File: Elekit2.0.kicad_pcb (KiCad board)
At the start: 2 copper layers, 100 x 58.5 mm, 55 parts, among them Q1 S8050, Q2 AO3401A, Q3 S8050, Q4 2N7002, SW1 SW_Push, U1 MY-2032-12, U2 TYPE-C_16PIN_2MD(073), U3 MY-2032-12, U4 74HC595, U5 XC6206P332MR, U6 TS-1187A-B-A-B, U7 TS-1187A-B-A-B, U8 ESP32-C3-WROOM-02-N4(4MB), U9 SRV05-4-P-T7

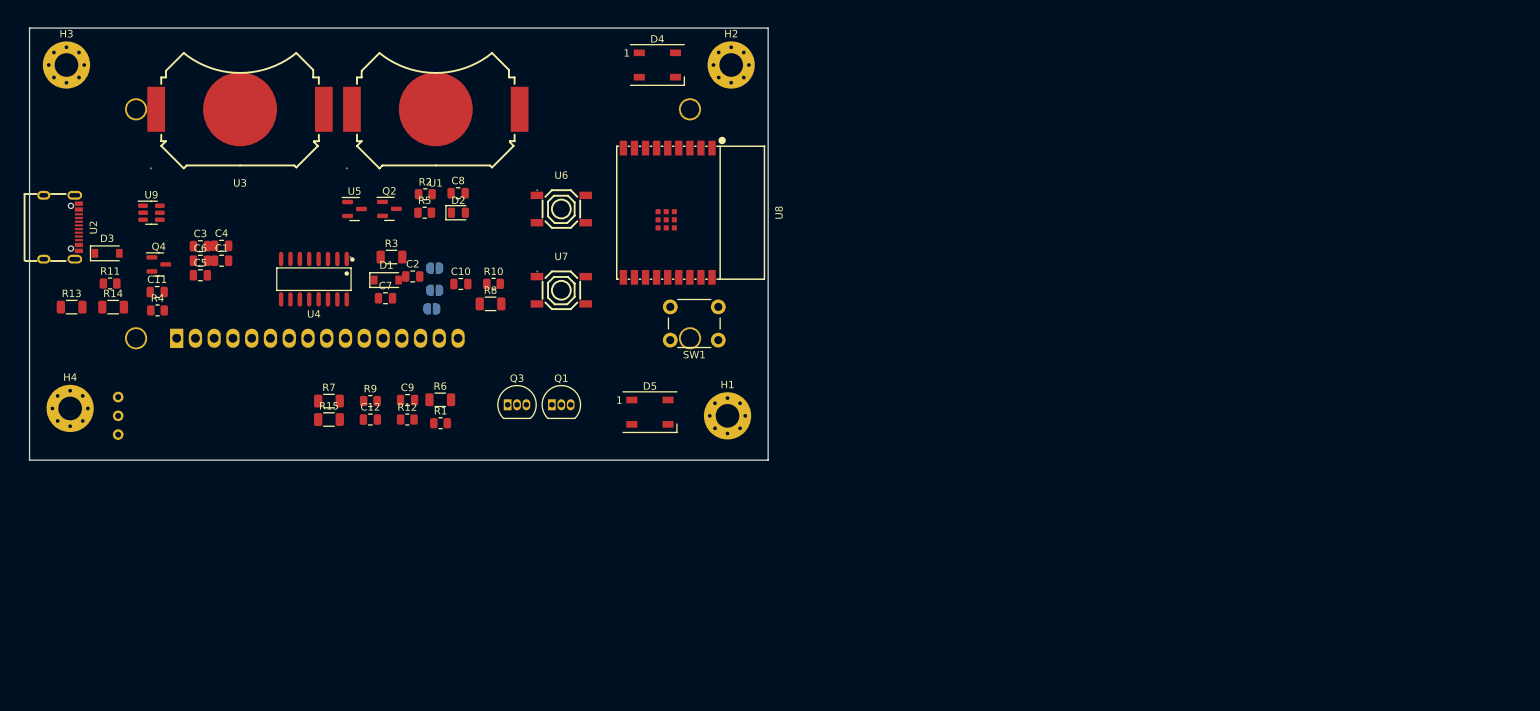
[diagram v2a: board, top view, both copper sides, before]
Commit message: Add H bridge motor controllers and create first draft of pcb
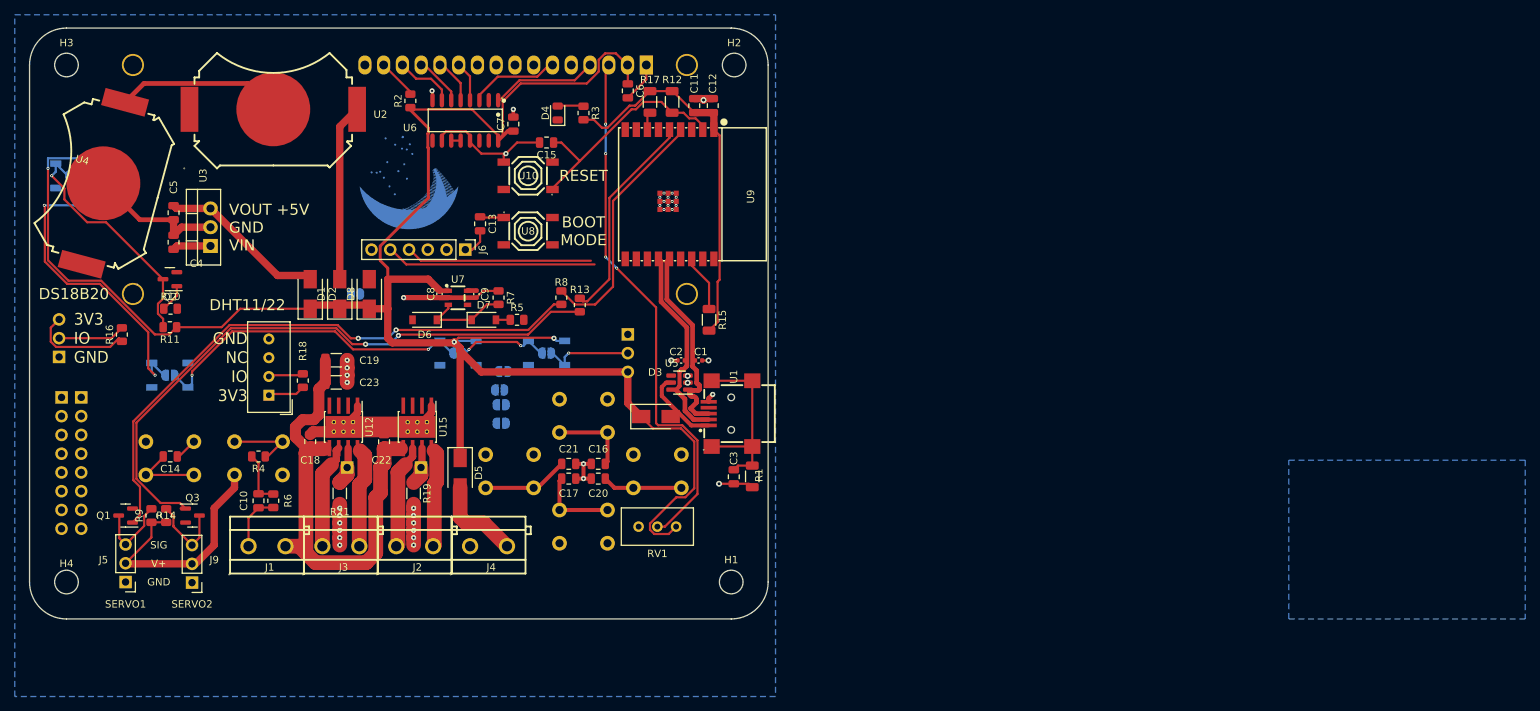
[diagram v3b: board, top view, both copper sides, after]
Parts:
- removed Q4: 2N7002, Package_TO_SOT_SMD:SOT-23
- added C13: 0.1u, Capacitor_SMD:C_0805_2012Metric, F.Cu at (81.0, 46.5)
- added C14: 0.1u, Capacitor_SMD:C_0805_2012Metric, F.Cu at (39.0, 78.0)
- added C15: 0.1u, Capacitor_SMD:C_0805_2012Metric, F.Cu at (90.0, 35.5)
- added C16: 0.1u, Capacitor_SMD:C_0805_2012Metric, F.Cu at (97.0, 79.0)
- added C17: 0.1u, Capacitor_SMD:C_0805_2012Metric, F.Cu at (93.0, 81.0)
- added C18: 0.1u, Capacitor_SMD:C_0805_2012Metric, F.Cu at (58.0, 76.0)
- added C19: 10u 50V, Capacitor_SMD:C_1206_3216Metric, F.Cu at (61.5, 65.0)
- added C20: 0.1u, Capacitor_SMD:C_0805_2012Metric, F.Cu at (97.0, 81.0)
- added C21: 0.1u, Capacitor_SMD:C_0805_2012Metric, F.Cu at (93.0, 79.0)
- added C22: 0.1u, Capacitor_SMD:C_0805_2012Metric, F.Cu at (68.0, 76.0)
- added C23: 10u 50V, Capacitor_SMD:C_1206_3216Metric, F.Cu at (61.5, 68.0)
- added D10: WS2812B, LED_SMD:LED_WS2812B_PLCC4_5.0x5.0mm_P3.2mm, B.Cu at (39.0, 67.0)
- added D11: WS2812B, LED_SMD:LED_WS2812B_PLCC4_5.0x5.0mm_P3.2mm, B.Cu at (78.0, 64.0)
- added D12: WS2812B, LED_SMD:LED_WS2812B_PLCC4_5.0x5.0mm_P3.2mm, B.Cu at (90.0, 64.0)
- added D6: 1N4148W, Diode_SMD:D_SOD-123, F.Cu at (73.5, 59.5)
- added D7: 1N4148W, Diode_SMD:D_SOD-123, F.Cu at (81.5, 59.5)
- added D8: SS34, Diode_SMD:D_SMA, F.Cu at (66.0, 56.0)
- added D9: WS2812B, LED_SMD:LED_WS2812B_PLCC4_5.0x5.0mm_P3.2mm, B.Cu at (26.0, 40.0)
- added J1: Screw_Terminal_01x02, 0_JLCPCB_Footprints:CONN-TH_P5.00_KF301-5.0-2P, F.Cu at (52.5, 90.0)
- added J10: Conn_01x03_Male, Connector_PinHeader_2.54mm:PinHeader_1x03_P2.54mm_Vertical, B.Cu at (101.0, 61.5)
- added J11: DS18B20 temperature sensor, Connector_PinHeader_2.54mm:PinHeader_1x03_P2.54mm_Vertical, B.Cu at (24.0, 64.5)
- added J12: Conn_01x01_Male, Connector_PinHeader_2.54mm:PinHeader_1x01_P2.54mm_Vertical, F.Cu at (63.0, 79.5)
- added J13: Conn_01x01_Male, 0_JLCPCB_Footprints:PinHeader_1x01_P2.54mm_Vertical, F.Cu at (73.0, 79.5)
- added J2: Screw_Terminal_01x02, 0_JLCPCB_Footprints:CONN-TH_P5.00_KF301-5.0-2P, F.Cu at (72.5, 90.0)
- added J3: Screw_Terminal_01x02, 0_JLCPCB_Footprints:CONN-TH_P5.00_KF301-5.0-2P, F.Cu at (62.5, 90.0)
- added J4: Screw_Terminal_01x02, 0_JLCPCB_Footprints:CONN-TH_P5.00_KF301-5.0-2P, F.Cu at (82.5, 90.0)
- added J5: Conn_01x03_Male, Connector_PinHeader_2.54mm:PinHeader_1x03_P2.54mm_Vertical, F.Cu at (33.0, 95.0)
- added J6: Conn_01x06_Male, Connector_PinHeader_2.54mm:PinHeader_1x06_P2.54mm_Vertical, F.Cu at (79.0, 50.0)
- added J7: Conn_01x08, Connector_PinHeader_2.54mm:PinHeader_1x08_P2.54mm_Vertical, B.Cu at (27.0, 70.0)
- added J8: Conn_01x08, Connector_PinHeader_2.54mm:PinHeader_1x08_P2.54mm_Vertical, B.Cu at (24.3, 70.0)
- added J9: Conn_01x03_Male, Connector_PinHeader_2.54mm:PinHeader_1x03_P2.54mm_Vertical, F.Cu at (42.0, 95.1)
- added JP4: Power LED, Jumper:SolderJumper-2_P1.3mm_Open_RoundedPad1.0x1.5mm, B.Cu at (83.7, 69.0)
- added JP5: led bypass, Jumper:SolderJumper-2_P1.3mm_Open_RoundedPad1.0x1.5mm, B.Cu at (64.2, 56.0)
- added JP6: led bypass, Jumper:SolderJumper-2_P1.3mm_Open_RoundedPad1.0x1.5mm, B.Cu at (26.0, 40.0)
- added JP7: led bypass, Jumper:SolderJumper-2_P1.3mm_Open_RoundedPad1.0x1.5mm, B.Cu at (39.0, 67.0)
- added JP8: led bypass, Jumper:SolderJumper-2_P1.3mm_Open_RoundedPad1.0x1.5mm, B.Cu at (78.0, 64.0)
- added JP9: led bypass, Jumper:SolderJumper-2_P1.3mm_Open_RoundedPad1.0x1.5mm, B.Cu at (90.0, 64.0)
- added LOGO1: CASTOR, 0_JLCPCB_Footprints:Castor logo, B.Cu at (78.5, 33.4)
- added R16: 4.7k, Resistor_SMD:R_0805_2012Metric, F.Cu at (32.5, 61.5)
- added R17: 10k, Resistor_SMD:R_1206_3216Metric, F.Cu at (104.0, 30.0)
- added R18: 10k, Resistor_SMD:R_0805_2012Metric, F.Cu at (57.0, 67.7)
- added R19: 0R, Resistor_SMD:R_1206_3216Metric, F.Cu at (72.0, 83.0)
- added R21: 0R, Resistor_SMD:R_1206_3216Metric, F.Cu at (62.0, 83.0)
- added SW2: SW_Push, Button_Switch_THT:SW_PUSH_6mm, B.Cu at (42.2, 76.0)
- added SW3: SW_Push, Button_Switch_THT:SW_PUSH_6mm, B.Cu at (98.2, 70.2)
- added SW4: SW_Push, Button_Switch_THT:SW_PUSH_6mm, B.Cu at (91.8, 89.8)
- added SW5: SW_Push, Button_Switch_THT:SW_PUSH_6mm, B.Cu at (108.2, 77.8)
- added SW6: SW_Push, Button_Switch_THT:SW_PUSH_6mm, B.Cu at (88.2, 77.8)
- added U10: TS-1187A-B-A-B, 0_JLCPCB_Footprints:SW-SMD_4P-L5.1-W5.1-P3.70-LS6.5-TL-2, F.Cu at (87.5, 40.0)
- added U11: DHT11, Sensor:Aosong_DHT11_5.5x12.0_P2.54mm, F.Cu at (52.4, 69.7)
- added U12: DRV8870DDA, Package_SO:Texas_HTSOP-8-1EP_3.9x4.9mm_P1.27mm_EP2.95x4.9mm_Mask2.4x3.1mm_ThermalVias, F.Cu at (62.5, 74.0)
- added U15: DRV8870DDA, Package_SO:Texas_HTSOP-8-1EP_3.9x4.9mm_P1.27mm_EP2.95x4.9mm_Mask2.4x3.1mm_ThermalVias, F.Cu at (72.5, 74.0)
- C1, C2: value 0.1u -> 0.1u 50V; footprint Capacitor_SMD:C_0805_2012Metric -> Capacitor_SMD:C_0402_1005Metric
- C10: value 0.1u -> 1u
- C3: value 0.1u -> 4.7n
- C4: value 4.7n -> 0.47u 50v
- C6, C7: value 1u -> 0.1u
- C8: value 1u -> 1u 25V; footprint Capacitor_SMD:C_0805_2012Metric -> Capacitor_SMD:C_0402_1005Metric
- C9: value 0.1u -> 1u 25V; footprint Capacitor_SMD:C_0805_2012Metric -> Capacitor_SMD:C_0402_1005Metric
- D1, D3: value B5819W -> SS34; footprint Diode_SMD:D_SOD-123 -> Diode_SMD:D_SMA
- D2: value LED -> SS34; footprint LED_SMD:LED_0805_2012Metric -> Diode_SMD:D_SMA
- D4: value WS2812B -> LED; footprint LED_SMD:LED_WS2812B_PLCC4_5.0x5.0mm_P3.2mm -> LED_SMD:LED_0805_2012Metric
- D5: value WS2812B -> SS34; footprint LED_SMD:LED_WS2812B_PLCC4_5.0x5.0mm_P3.2mm -> Diode_SMD:D_SMA
- H1, H2, H3, H4: footprint MountingHole:MountingHole_3.2mm_M3_Pad_Via -> MountingHole:MountingHole_3.2mm_M3
- JP1: value Power LED -> Latch bypass
- JP2: value Latch bypass -> VIN DIODE BYPASS
- JP3: value Power latch -> Latch control
- Q1, Q3: value S8050 -> 2N7002; footprint Package_TO_SOT_THT:TO-92_Inline -> Package_TO_SOT_SMD:SOT-23
- Q2: value AO3401A -> 2N7002
- R1: value 1k -> 1M; footprint Resistor_SMD:R_0805_2012Metric -> Resistor_SMD:R_1206_3216Metric
- R11: value 1k -> 5.1k
- R12: value 5.1k -> 10k; footprint Resistor_SMD:R_0805_2012Metric -> Resistor_SMD:R_1206_3216Metric
- R13, R14, R8: value 10k -> 1k; footprint Resistor_SMD:R_1206_3216Metric -> Resistor_SMD:R_0805_2012Metric
- R2: value 5.1k -> 220R
- R3: value 1M -> 1k; footprint Resistor_SMD:R_1206_3216Metric -> Resistor_SMD:R_0805_2012Metric
- R4: value 220R -> 10k
- R5: value 5.1k -> 1k
- R6: footprint Resistor_SMD:R_1206_3216Metric -> Resistor_SMD:R_0805_2012Metric
- R7: value 10k -> 1M; footprint Resistor_SMD:R_1206_3216Metric -> Resistor_SMD:R_0805_2012Metric
- RV1: moved to F.Cu
- SW1: moved to B.Cu
- U1: value MY-2032-12 -> MINI_5PTP; footprint 0_JLCPCB_Footprints:BAT-SMD_MY-2032-12 -> 0_JLCPCB_Footprints:MINI-USB-SMD_MINI-5PTP
- U2: value TYPE-C_16PIN_2MD(073) -> MY-2032-12; footprint 0_JLCPCB_Footprints:USB-C-SMD_TYPE-C-6PIN-2MD-073 -> 0_JLCPCB_Footprints:BAT-SMD_MY-2032-12
- U3: value MY-2032-12 -> L7805; footprint 0_JLCPCB_Footprints:BAT-SMD_MY-2032-12 -> Package_TO_SOT_THT:TO-220-3_Vertical
- U4: value 74HC595 -> MY-2032-12; footprint 0_JLCPCB_Footprints:SOIC-16_L9.9-W3.9-P1.27-LS6.0-BL -> 0_JLCPCB_Footprints:BAT-SMD_MY-2032-12
- U5: value XC6206P332MR -> SRV05-4-P-T7; footprint Package_TO_SOT_SMD:SOT-23 -> Package_TO_SOT_SMD:SOT-23-6
- U6: value TS-1187A-B-A-B -> 74HC595; footprint 0_JLCPCB_Footprints:SW-SMD_4P-L5.1-W5.1-P3.70-LS6.5-TL-2 -> 0_JLCPCB_Footprints:SOIC-16_L9.9-W3.9-P1.27-LS6.0-BL
- U7: value TS-1187A-B-A-B -> ME6211C33M5G-N; footprint 0_JLCPCB_Footprints:SW-SMD_4P-L5.1-W5.1-P3.70-LS6.5-TL-2 -> 0_JLCPCB_Footprints:SOT-23-5_L3.0-W1.7-P0.95-LS2.8-BR
- U8: value ESP32-C3-WROOM-02-N4(4MB) -> TS-1187A-B-A-B; footprint 0_JLCPCB_Footprints:BULETM-SMD_ESPRESSIF_ESP32-C3-WROOM-02-N4-4MB -> 0_JLCPCB_Footprints:SW-SMD_4P-L5.1-W5.1-P3.70-LS6.5-TL-2
- U9: value SRV05-4-P-T7 -> ESP32-C3-WROOM-02-N4(4MB); footprint Package_TO_SOT_SMD:SOT-23-6 -> 0_JLCPCB_Footprints:BULETM-SMD_ESPRESSIF_ESP32-C3-WROOM-02-N4-4MB
- moved C3 78.7 mm to (115.4, 80.8), turned to -90 degrees
- moved D3 77.5 mm to (104.8, 72.6)
- moved C11 77.0 mm to (110.0, 30.5), turned to 90 degrees
- moved DS1 73.6 mm to (103.5, 25.0), turned to 180 degrees
- moved RV1 71.6 mm to (102.5, 87.5), turned to 180 degrees
- moved U9 70.2 mm to (106.6, 42.5), turned to -90 degrees
- moved R13 68.8 mm to (94.5, 57.5), turned to 90 degrees
- moved C1 66.0 mm to (110.6, 65.0)
- moved C12 62.9 mm to (112.5, 30.5), turned to -90 degrees
- moved C6 62.3 mm to (101.0, 28.5), turned to -90 degrees
- moved SW1 60.6 mm to (54.2, 76.0)
- moved Q1 59.6 mm to (33.0, 86.0), turned to 180 degrees
- moved U1 57.2 mm to (114.9, 72.2), turned to 90 degrees
- moved R12 56.0 mm to (107.0, 30.0), turned to 90 degrees
- moved R15 53.2 mm to (112.0, 59.5), turned to -90 degrees
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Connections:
- C1 pad 1: /VBUS -> /D+
- C10 pad 1: /CHIP_PU -> /BTN
- C12 pad 1: +3.3V -> GND
- C12 pad 2: GND -> +3.3V
- C2 pad 2: /D+ -> /D-
- C3 pad 1: GND -> Net-(C3-Pad1)
- C3 pad 2: /D- -> GND
- C4 pad 1: Net-(C4-Pad1) -> GND
- C4 pad 2: GND -> /HVBUS
- C5 pad 1: /VBUS -> GND
- C5 pad 2: GND -> Net-(C5-Pad2)
- C6 pad 1: Net-(C6-Pad1) -> /VBUS
- C7 pad 1: Net-(C7-Pad1) -> /VBUS
- C8 pad 1: +3.3V -> GND
- C8 pad 2: GND -> /VBUS
- C9 pad 1: /GPIO9 -> +3.3V
- D2 pad 1: GND -> /VBUS
- D2 pad 2: Net-(D2-Pad2) -> Net-(C5-Pad2)
- D4 pad 1: /VBUS -> Net-(D4-Pad1)
- D5 pad 2: unconnected-(D5-Pad2) -> Net-(D5-Pad2)
- JP1 pad 1: Net-(D2-Pad2) -> /EN_LDO
- JP1 pad 2: Net-(JP1-Pad2) -> /VBUS
- JP2 pad 1: Net-(C6-Pad1) -> /VBUS
- JP2 pad 2: /VBUS -> Net-(D5-Pad2)
- JP3 pad 1: /GPIO4 -> Net-(JP3-Pad1)
- JP3 pad 2: Net-(JP3-Pad2) -> /GPIO4
- Q1 pad 1: /RTS -> Net-(Q1-Pad1)
- Q1 pad 2: Net-(Q1-Pad2) -> GND
- Q1 pad 3: /CHIP_PU -> /SERVO1
- Q2 pad 1: Net-(C7-Pad1) -> Net-(Q2-Pad1)
- Q2 pad 2: /VBUS -> GND
- Q2 pad 3: Net-(C6-Pad1) -> Net-(D9-Pad4)
- Q3 pad 1: /DTR -> Net-(Q3-Pad1)
- Q3 pad 2: Net-(Q3-Pad2) -> GND
- Q3 pad 3: /GPIO9 -> /SERVO2
- R1 pad 1: Net-(JP1-Pad2) -> Net-(C3-Pad1)
- R1 pad 2: +3.3V -> GND
- R10 pad 1: Net-(C7-Pad1) -> Net-(Q2-Pad1)
- R10 pad 2: Net-(JP3-Pad2) -> /GPIO5
- R11 pad 1: Net-(Q4-Pad1) -> /VBUS
- R11 pad 2: /GPIO5 -> Net-(D9-Pad4)
- R12 pad 1: /VBUS -> /CHIP_PU
- R12 pad 2: Net-(D4-Pad4) -> +3.3V
- R13 pad 1: /CHIP_PU -> Net-(Q3-Pad1)
- R13 pad 2: +3.3V -> /GPIO6
- R14 pad 1: /GPIO2 -> /VBUS
- R14 pad 2: +3.3V -> /SERVO2
- R15 pad 1: /GPIO8 -> /GPIO2
- R2 pad 1: GND -> /VBUS
- R2 pad 2: Net-(R2-Pad2) -> Net-(DS1-Pad15)
- R3 pad 1: Net-(C4-Pad1) -> Net-(D4-Pad2)
- R3 pad 2: GND -> +3.3V
- R4 pad 1: /VBUS -> Net-(R4-Pad1)
- R4 pad 2: Net-(DS1-Pad15) -> /BTN
- R5 pad 1: GND -> Net-(D7-Pad2)
- R5 pad 2: Net-(R5-Pad2) -> Net-(JP3-Pad1)
- R6 pad 1: Net-(Q1-Pad2) -> /BTN
- R6 pad 2: /DTR -> GND
- R7 pad 1: Net-(C7-Pad1) -> GND
- R7 pad 2: /VBUS -> /EN_LDO
- R8 pad 1: Net-(Q3-Pad2) -> Net-(Q1-Pad1)
- R8 pad 2: /RTS -> /GPIO5
- R9 pad 1: Net-(C7-Pad1) -> /VBUS
- R9 pad 2: Net-(R9-Pad2) -> /SERVO1
- SW1 pad 1: GND -> Net-(R4-Pad1)
- SW1 pad 2: Net-(R9-Pad2) -> /VBUS
- U1 pad 1: +BATT -> /VUSB
- U1 pad 2: Net-(U1-Pad2) -> /D-
- U2 pad 1: GND -> +BATT
- U2 pad 2: /VUSB -> Net-(U2-Pad2)
- U3 pad 1: Net-(U1-Pad2) -> /HVBUS
- U4 pad 1: Net-(DS1-Pad4) -> Net-(U2-Pad2)
- U4 pad 2: unconnected-(U4-Pad2) -> GND
- U5 pad 1: GND -> /D+
- U5 pad 2: +3.3V -> GND
- U5 pad 3: Net-(C6-Pad1) -> unconnected-(U5-Pad3)
- U6 pad 1: /GPIO9 -> Net-(DS1-Pad4)
- U6 pad 3: unconnected-(U6-Pad3) -> Net-(DS1-Pad6)
- U6 pad 4: GND -> Net-(DS1-Pad11)
- U7 pad 1: /CHIP_PU -> /VBUS
- U7 pad 2: unconnected-(U7-Pad2) -> GND
- U7 pad 3: unconnected-(U7-Pad3) -> /EN_LDO
- U7 pad 4: GND -> unconnected-(U7-Pad4)
- U8 pad 1: +3.3V -> /GPIO9
- U8 pad 2: /CHIP_PU -> unconnected-(U8-Pad2)
- U8 pad 3: /GPIO4 -> unconnected-(U8-Pad3)
- U8 pad 4: /GPIO5 -> GND
- U9 pad 1: /D+ -> +3.3V
- U9 pad 2: GND -> /CHIP_PU
- U9 pad 3: /D- -> /GPIO4
- U9 pad 4: unconnected-(U9-Pad4) -> /GPIO5
- U9 pad 5: /VUSB -> /GPIO6
- U9 pad 6: unconnected-(U9-Pad6) -> /GPIO7
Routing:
- net /VBUS: track 0.00 -> 297.8 mm, vias 0 -> 3
- net GND: track 0.00 -> 136.2 mm, vias 0 -> 40
- net Net-(Q3-Pad1): track 0.00 -> 84.6 mm, vias 0 -> 2
- net Net-(Q1-Pad1): track 0.00 -> 80.6 mm, vias 0 -> 2
- net Net-(DS1-Pad3): track 0.00 -> 72.6 mm, vias 0 -> 4
- net +3.3V: track 0.00 -> 72.0 mm
- net /HVBUS: track 0.00 -> 67.6 mm
- net Net-(D10-Pad4): track 0.00 -> 46.0 mm, vias 0 -> 2
- net Net-(D10-Pad2): track 0.00 -> 44.6 mm, vias 0 -> 2
- net /GPIO5: track 0.00 -> 33.8 mm
- net Net-(D9-Pad4): track 0.00 -> 33.2 mm, vias 0 -> 1
- net /CHIP_PU: track 0.00 -> 31.8 mm
- net /GPIO6: track 0.00 -> 29.0 mm
- net /TX: track 0.00 -> 28.5 mm
- net /D-: track 0.00 -> 27.1 mm
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- added copper zone on B.Cu, net GND
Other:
- board size 100 x 58.5 mm -> 100 x 80 mm
- board text added: "3V3 IO GND"
- board text added: "BOOT MODE"
- board text added: "DHT11/22"
- board text added: "DS18B20"
- board text added: "GND"
- board text added: "GND NC IO 3V3"
- board text added: "RESET"
- board text added: "SERVO1"
- board text added: "SERVO2"
- board text added: "SIG"
- board text added: "V+"
- board text added: "VOUT +5V GND VIN"

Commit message: Create first complete version
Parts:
- removed C10: 1u, Capacitor_SMD:C_0805_2012Metric
- removed J7, J8: Conn_01x08, Connector_PinHeader_2.54mm:PinHeader_1x08_P2.54mm_Vertical
- added C24: 0.1u 50V, Capacitor_SMD:C_0402_1005Metric, F.Cu at (80.5, 71.5)
- added C25: 1u, Capacitor_SMD:C_0805_2012Metric, F.Cu at (78.0, 84.5)
- added C26: C_Polarized, Capacitor_THT:CP_Radial_D5.0mm_P2.00mm, B.Cu at (22.0, 48.5)
- added JP10: Servo1, Jumper:SolderJumper-2_P1.3mm_Open_RoundedPad1.0x1.5mm, B.Cu at (38.2, 56.4)
- added JP11: Servo1, Jumper:SolderJumper-2_P1.3mm_Open_RoundedPad1.0x1.5mm, B.Cu at (38.2, 59.4)
- added JP12: Servo1, Jumper:SolderJumper-2_P1.3mm_Open_RoundedPad1.0x1.5mm, B.Cu at (38.2, 50.4)
- added JP13: Servo1, Jumper:SolderJumper-2_P1.3mm_Open_RoundedPad1.0x1.5mm, B.Cu at (38.2, 53.4)
- added JP14: Latch control, Jumper:SolderJumper-2_P1.3mm_Open_RoundedPad1.0x1.5mm, B.Cu at (38.0, 47.4)
- added R20: 1k, Resistor_SMD:R_0402_1005Metric, F.Cu at (82.0, 85.0)
- added R22: 10k, Resistor_SMD:R_0402_1005Metric, F.Cu at (82.0, 83.0)
- added R23: 1k, Resistor_SMD:R_0402_1005Metric, F.Cu at (83.5, 85.0)
- added R24: 1k, Resistor_SMD:R_0402_1005Metric, F.Cu at (85.0, 85.0)
- added R25: 1k, Resistor_SMD:R_0402_1005Metric, F.Cu at (88.0, 85.0)
- added R26: 1k, Resistor_SMD:R_0402_1005Metric, F.Cu at (86.5, 85.0)
- added R28: 10k, Resistor_SMD:R_0402_1005Metric, F.Cu at (83.5, 83.0)
- added R29: 10k, Resistor_SMD:R_0402_1005Metric, F.Cu at (85.0, 83.0)
- added R30: 10k, Resistor_SMD:R_0402_1005Metric, F.Cu at (88.0, 83.0)
- added R33: 10k, Resistor_SMD:R_0402_1005Metric, F.Cu at (86.5, 83.0)
- added U13: 74HC165, 0_JLCPCB_Footprints:SOIC-16_L9.9-W3.9-P1.27-LS6.0-BL, F.Cu at (80.5, 77.0)
- C12, C13, C14, C15, C16, C17, C18, C20, C21, C22, C5, C6, C7: value 0.1u -> 0.1u 50V; footprint Capacitor_SMD:C_0805_2012Metric -> Capacitor_SMD:C_0402_1005Metric
- DS1: footprint Display:WC1602A -> SnapEDA Library:LCD_RC1602B-BIW-CSV
- J1, J2, J3, J4, J5, J6, J9, U11: moved to B.Cu
- J12: footprint Connector_PinHeader_2.54mm:PinHeader_1x01_P2.54mm_Vertical -> 0_JLCPCB_Footprints:PinHeader_1x01_P2.54mm_Vertical
- JP2, JP5: moved to F.Cu
- JP3: value Latch control -> H-Bridge
- JP4: value Power LED -> PWR LED
- R10, R13, R14, R18, R3, R5, R6, R8, R9: footprint Resistor_SMD:R_0805_2012Metric -> Resistor_SMD:R_0402_1005Metric
- R12, R15, R17: footprint Resistor_SMD:R_1206_3216Metric -> Resistor_SMD:R_0402_1005Metric
- R4: value 10k -> 1k; footprint Resistor_SMD:R_0805_2012Metric -> Resistor_SMD:R_0402_1005Metric
- moved J5 100.1 mm to (104.0, 24.5)
- moved Q1 88.3 mm to (104.0, 33.5), turned to 90 degrees
- moved J9 88.3 mm to (95.0, 24.5)
- moved J10 86.0 mm to (20.0, 32.5)
- moved R9 83.4 mm to (100.0, 32.0), turned to -90 degrees
- moved R14 80.7 mm to (98.5, 32.0), turned to -90 degrees
- moved Q3 74.5 mm to (94.9, 33.5), turned to 90 degrees
- moved J4 65.9 mm to (22.0, 64.0), turned to 90 degrees
- moved JP2 64.4 mm to (21.5, 55.0), turned to -90 degrees
- moved LOGO1 55.1 mm to (71.5, 88.0)
- moved JP1 54.1 mm to (38.2, 44.4)
- moved D5 54.1 mm to (28.5, 59.0)
- moved D11 53.6 mm to (78.0, 27.0), turned to 0 degrees
- moved JP8 53.6 mm to (78.0, 27.0), turned to 180 degrees
- moved J11 52.4 mm to (63.0, 29.5)
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- renumbered D12 to D10, D9 to D11, D10 to D12, D11 to D9, JP8 to JP6, JP9 to JP7, JP6 to JP8, JP7 to JP9
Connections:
- net /BTN renamed /BTN1
- C14 pad 1: GND -> /VBUS
- C14 pad 2: Net-(C14-Pad2) -> GND
- C16 pad 1: GND -> /BTN2
- C16 pad 2: Net-(C16-Pad2) -> /VBUS
- C17 pad 1: GND -> /BTN3
- C17 pad 2: Net-(C17-Pad2) -> /VBUS
- C20 pad 1: GND -> /BTN4
- C20 pad 2: Net-(C20-Pad2) -> /VBUS
- C21 pad 1: GND -> /BTN5
- C21 pad 2: Net-(C21-Pad2) -> /VBUS
- D10 pad 2: Net-(D12-Pad2) -> Net-(D10-Pad2)
- D11 pad 4: Net-(D9-Pad4) -> Net-(D10-Pad2)
- D12 pad 2: Net-(D10-Pad2) -> Net-(D12-Pad2)
- D9 pad 4: Net-(D10-Pad2) -> Net-(D9-Pad4)
- J2 pad 1: /A1 -> /A2
- J2 pad 2: /A2 -> /A1
- J3 pad 1: /B1 -> /B2
- J3 pad 2: /B2 -> /B1
- JP3 pad 1: Net-(JP3-Pad1) -> +3.3V
- JP3 pad 2: /GPIO4 -> /H-BRIDGE_PWR
- JP6 pad 1: Net-(D10-Pad2) -> Net-(D9-Pad4)
- JP7 pad 2: Net-(D12-Pad2) -> Net-(D10-Pad2)
- JP8 pad 1: Net-(D9-Pad4) -> Net-(D10-Pad2)
- JP9 pad 2: Net-(D10-Pad2) -> Net-(D12-Pad2)
- R10 pad 2: /GPIO5 -> /GPIO2
- R13 pad 2: /GPIO6 -> /SERVO2_c
- R5 pad 2: Net-(JP3-Pad1) -> /Latch control
- R8 pad 2: /GPIO5 -> /SERVO1_c
- SW2 pad 1: GND -> /VBUS
- SW2 pad 2: Net-(C14-Pad2) -> Net-(R20-Pad1)
- SW3 pad 1: GND -> /VBUS
- SW3 pad 2: Net-(C16-Pad2) -> Net-(R23-Pad1)
- SW4 pad 1: GND -> /VBUS
- SW4 pad 2: Net-(C17-Pad2) -> Net-(R24-Pad1)
- SW5 pad 1: GND -> /VBUS
- SW5 pad 2: Net-(C20-Pad2) -> Net-(R25-Pad1)
- SW6 pad 1: GND -> /VBUS
- SW6 pad 2: Net-(C21-Pad2) -> Net-(R26-Pad1)
- U12 pad 4: +3.3V -> /H-BRIDGE_PWR
- U15 pad 4: +3.3V -> /H-BRIDGE_PWR
- U6 pad 11: Net-(U6-Pad11) -> /CLK2
- U6 pad 12: Net-(U6-Pad11) -> /CLK2
- U6 pad 14: unconnected-(U6-Pad14) -> /RX
- U9 pad 10: /GPIO10 -> /CLK1
- U9 pad 15: /GPIO3 -> /CLK2
- U9 pad 3: /GPIO4 -> /B1_c
- U9 pad 4: /GPIO5 -> /B2_C
- U9 pad 5: /GPIO6 -> /A1_c
- U9 pad 6: /GPIO7 -> /A2_C
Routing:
- net /VBUS: track 297.8 -> 648.2 mm, vias 3 -> 17
- net /B1_c: track 0.00 -> 187.2 mm, vias 0 -> 3
- net +3.3V: track 72.0 -> 185.2 mm, vias 0 -> 6
- net /GPIO2: track 7.76 -> 118.9 mm, vias 0 -> 6
- net /GPIO0: track 0.00 -> 90.9 mm, vias 0 -> 3
- net /A1_c: track 0.00 -> 88.1 mm
- net /B2_C: track 0.00 -> 87.8 mm
- net /A2_C: track 0.00 -> 86.7 mm
- net /GPIO1: track 0.00 -> 85.5 mm, vias 0 -> 3
- net /H-BRIDGE_PWR: track 0.00 -> 83.0 mm, vias 0 -> 3
- net /SERVO2_c: track 0.00 -> 83.0 mm, vias 0 -> 1
- net /HVBUS: track 67.6 -> 147.4 mm
- net Net-(Q3-Pad1): track 84.6 -> 4.98 mm, vias 2 -> 0
- net /SERVO1_c: track 0.00 -> 77.7 mm, vias 0 -> 1
- net Net-(Q1-Pad1): track 80.6 -> 3.43 mm, vias 2 -> 0
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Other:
- board size 100 x 80 mm -> 100 x 100 mm
- board text added: "A1"
- board text added: "A2"
- board text added: "B1"
- board text added: "B2"
- board text added: "Constant PWR"
- board text added: "H-Bridge PWR"
- board text added: "IO0"
- board text added: "IO1"
- board text added: "IO4"
- board text added: "PWR"
- board text added: "PWR LED"
- board text added: "PWR Latch"
- board text added: "VIN"
- board text added: "VIN 5-6V"
- board text added: "VIN GND VOUT +5V"
- board text added: "VOUT"
- board text removed: "VOUT +5V GND VIN"

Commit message: production updates
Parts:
- removed C3: 4.7n, Capacitor_SMD:C_0805_2012Metric
- removed R1: 1M, Resistor_SMD:R_1206_3216Metric
- added J7: Conn_01x04, Connector_PinSocket_2.54mm:PinSocket_1x04_P2.54mm_Vertical, F.Cu at (55.2, 70.0)
- moved C18 0.25 mm to (37.4, 76.6)
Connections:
- U1 pad 6: Net-(C3-Pad1) -> unconnected-(U1-Pad6)
- U1 pad 7: Net-(C3-Pad1) -> unconnected-(U1-Pad7)
- U1 pad 8: Net-(C3-Pad1) -> unconnected-(U1-Pad8)
- U1 pad 9: Net-(C3-Pad1) -> unconnected-(U1-Pad9)
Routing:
- net /B1_c: track 187.2 -> 148.7 mm
- net /H-BRIDGE_PWR: track 83.0 -> 49.8 mm
- net +3.3V: track 185.2 -> 216.9 mm
- net Net-(C3-Pad1): track 15.6 -> 0.00 mm
- net /GPIO0: track 90.9 -> 96.1 mm
- net /GPIO1: track 85.5 -> 90.3 mm
- net /HVBUS: track 147.4 -> 144.9 mm
- net GND: track 102.3 -> 100.2 mm, vias 56 -> 55
- net Net-(D4-Pad1): track 66.2 -> 66.7 mm
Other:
- board text added: "GND IO0 IO1 3V3"
